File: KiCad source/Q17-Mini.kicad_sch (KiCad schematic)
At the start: 80 parts, among them J1 Input, J2-1 SPK+, J2-2 SPK-, J3-1 V+, J3-2 GND, J3-3 V-, Q1 IRF610, Q10 KSA992, Q11 ZVP2106A, Q12 BD139, Q13 IRF610, Q14 IRF9610, Q15 FQA46N15, Q16 FQA36P15, Q2 KSA992, Q3 KSC1845, Q4 IRF9610, Q5 FQP3P20, Q6 FQP3N30, Q7 KSC1845, Q8 ZVN4206AV, Q9 ZVP2106A, U1 OPA1641

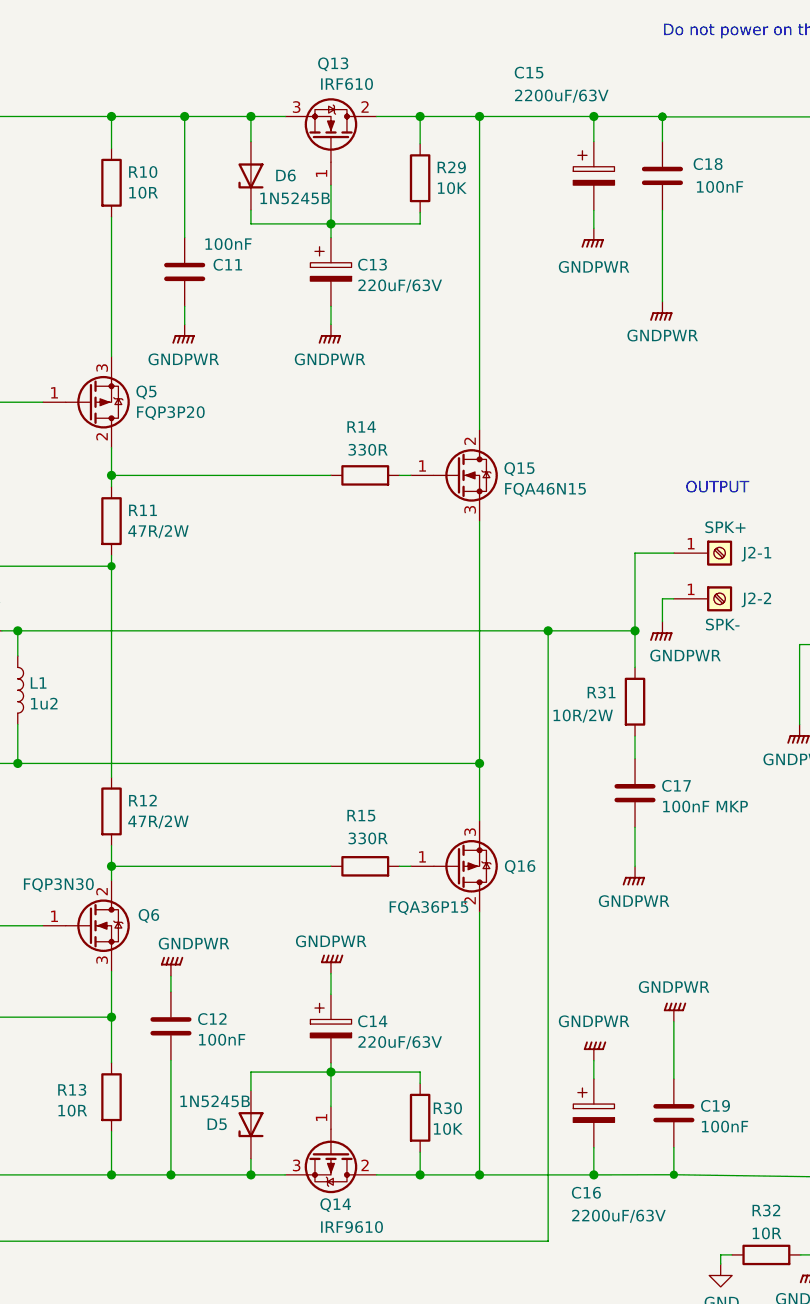
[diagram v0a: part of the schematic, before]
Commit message: Update Q17-Mini diagram
New 100R value for R29 and R30.
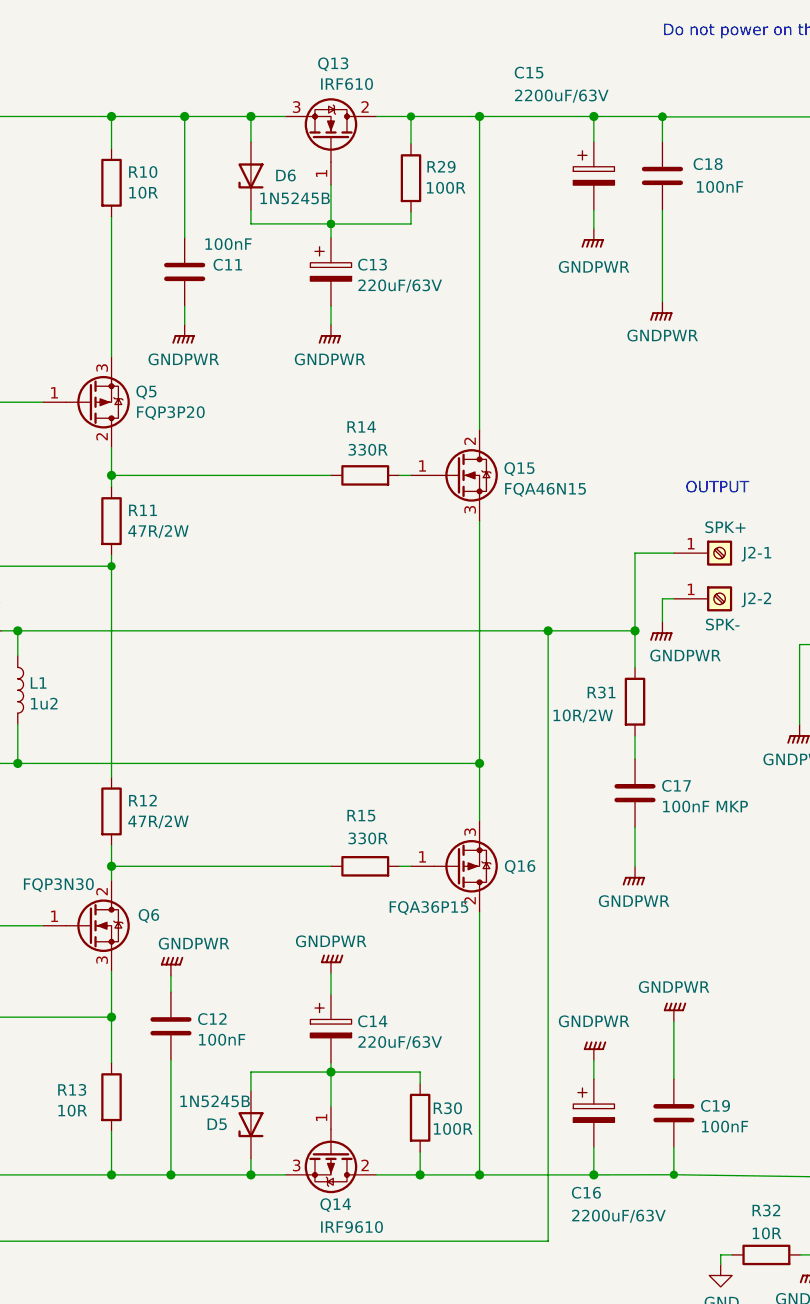
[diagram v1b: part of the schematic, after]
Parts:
- R29, R30: value 10K -> 100R
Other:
- moved on the sheet: R29
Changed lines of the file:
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@@
   (title_block
     (title "Q17-Mini Amplifier")
-    (date "2021-12-14")
-    (rev "1.1.4")
+    (date "2021-12-18")
+    (rev "1.1.5")
     (company "by eng. Tiberiu Vicol")
     (comment 1 "Modified by Stef for the Q17-Mini project")
@@
   (junction (at 49.53 103.124) (diameter 1.016) (color 0 0 0 0)
   )
+  (junction (at 203.2 35.8194) (diameter 0) (color 0 0 0 0)
+  )
   (junction (at 147.32 95.758) (diameter 1.016) (color 0 0 0 0)
   )
@@
   (junction (at 138.43 39.116) (diameter 1.016) (color 0 0 0 0)
   )
+  (junction (at 203.2 35.814) (diameter 0) (color 0 0 0 0)
+  )
   (junction (at 232.41 141.478) (diameter 1.016) (color 0 0 0 0)
   )
@@
   (junction (at 219.71 23.876) (diameter 1.016) (color 0 0 0 0)
   )
-  (junction (at 203.2 35.814) (diameter 1.016) (color 0 0 0 0)
-  )
   (junction (at 138.43 55.626) (diameter 1.016) (color 0 0 0 0)
   )
@@
   (junction (at 186.944 23.876) (diameter 1.016) (color 0 0 0 0)
   )
+  (junction (at 212.09 23.876) (diameter 0) (color 0 0 0 0)
+  )
   (junction (at 92.71 141.478) (diameter 1.016) (color 0 0 0 0)
   )
@@
   )
   (junction (at 42.672 73.914) (diameter 1.016) (color 0 0 0 0)
-  )
-  (junction (at 213.106 23.876) (diameter 1.016) (color 0 0 0 0)
   )
   (junction (at 241.3 141.4597) (diameter 0) (color 0 0 0 0)
@@
     (stroke (width 0) (type solid) (color 0 0 0 0))
   )
-  (wire (pts (xy 213.106 23.876) (xy 213.106 26.924))
-    (stroke (width 0) (type solid) (color 0 0 0 0))
-  )
   (wire (pts (xy 49.53 96.774) (xy 49.53 103.124))
     (stroke (width 0) (type solid) (color 0 0 0 0))
@@
   )
   (wire (pts (xy 203.2 44.958) (xy 203.2 46.99))
-    (stroke (width 0) (type solid) (color 0 0 0 0))
-  )
-  (wire (pts (xy 203.2 31.496) (xy 203.2 35.814))
-    (stroke (width 0) (type solid) (color 0 0 0 0))
-  )
-  (wire (pts (xy 203.2 35.814) (xy 203.2 37.338))
-    (stroke (width 0) (type solid) (color 0 0 0 0))
-  )
-  (wire (pts (xy 203.2 35.814) (xy 213.106 35.814))
-    (stroke (width 0) (type solid) (color 0 0 0 0))
-  )
-  (wire (pts (xy 213.106 35.814) (xy 213.106 34.544))
     (stroke (width 0) (type solid) (color 0 0 0 0))
   )
@@
     (stroke (width 0) (type solid) (color 0 0 0 0))
   )
-  (wire (pts (xy 219.71 23.876) (xy 213.106 23.876))
-    (stroke (width 0) (type solid) (color 0 0 0 0))
-  )
   (wire (pts (xy 219.71 58.674) (xy 219.71 23.876))
     (stroke (width 0) (type solid) (color 0 0 0 0))
   )
-  (wire (pts (xy 213.106 23.876) (xy 208.28 23.876))
+  (wire (pts (xy 208.28 23.876) (xy 212.09 23.876))
     (stroke (width 0) (type solid) (color 0 0 0 0))
   )
@@
     (stroke (width 0) (type solid) (color 0 0 0 0))
   )
+  (wire (pts (xy 203.2 31.496) (xy 203.2 35.814))
+    (stroke (width 0) (type default) (color 0 0 0 0))
+  )
   (wire (pts (xy 260.35 88.9) (xy 260.35 141.732))
     (stroke (width 0) (type solid) (color 0 0 0 0))
@@
     (stroke (width 0) (type solid) (color 0 0 0 0))
   )
+  (wire (pts (xy 212.09 35.8194) (xy 212.0909 34.5405))
+    (stroke (width 0) (type default) (color 0 0 0 0))
+  )
   (wire (pts (xy 116.332 80.01) (xy 116.332 83.312))
     (stroke (width 0) (type solid) (color 0 0 0 0))
@@
   )
   (wire (pts (xy 67.818 23.876) (xy 78.994 23.876))
+    (stroke (width 0) (type solid) (color 0 0 0 0))
+  )
+  (wire (pts (xy 212.09 23.876) (xy 219.71 23.876))
     (stroke (width 0) (type solid) (color 0 0 0 0))
   )
@@
     (stroke (width 0) (type solid) (color 0 0 0 0))
   )
+  (wire (pts (xy 203.2 35.8194) (xy 212.09 35.8194))
+    (stroke (width 0) (type default) (color 0 0 0 0))
+  )
   (wire (pts (xy 67.818 141.478) (xy 78.994 141.478))
     (stroke (width 0) (type solid) (color 0 0 0 0))
@@
   (wire (pts (xy 78.994 117.856) (xy 78.994 116.586))
     (stroke (width 0) (type solid) (color 0 0 0 0))
+  )
+  (wire (pts (xy 203.2 35.8194) (xy 203.2 37.338))
+    (stroke (width 0) (type default) (color 0 0 0 0))
   )
   (wire (pts (xy 150.368 55.626) (xy 150.368 58.166))
@@
     (stroke (width 0) (type solid) (color 0 0 0 0))
   )
+  (wire (pts (xy 203.2 35.814) (xy 203.2 35.8194))
+    (stroke (width 0) (type default) (color 0 0 0 0))
+  )
   (wire (pts (xy 178.816 73.8461) (xy 178.816 97.282))
     (stroke (width 0) (type solid) (color 0 0 0 0))
@@
   (wire (pts (xy 116.332 93.472) (xy 116.332 95.758))
     (stroke (width 0) (type solid) (color 0 0 0 0))
+  )
+  (wire (pts (xy 212.0909 26.9205) (xy 212.09 23.876))
+    (stroke (width 0) (type default) (color 0 0 0 0))
   )
   (wire (pts (xy 186.944 44.958) (xy 186.944 46.99))
@@
     (pin "1")
   )
-  (symbol (lib_id "Device:R") (at 213.106 30.734 0) (unit 1)
-    (in_bom yes) (on_board yes)
-    (property "Reference" "R29" (id 0) (at 214.8841 29.5846 0)
-      (effects (font (size 1.27 1.27)) (justify left))
-    )
-    (property "Value" "10K" (id 1) (at 214.884 31.883 0)
-      (effects (font (size 1.27 1.27)) (justify left))
-    )
-    (property "Footprint" "Resistor_THT:R_Axial_DIN0207_L6.3mm_D2.5mm_P10.16mm_Horizontal" (id 2) (at 211.328 30.734 90)
-      (effects (font (size 1.27 1.27)) hide)
-    )
-    (property "Datasheet" "~" (id 3) (at 213.106 30.734 0)
+  (symbol (lib_id "Device:R") (at 212.0909 30.7305 0) (unit 1)
+    (in_bom yes) (on_board yes)
+    (property "Reference" "R29" (id 0) (at 213.7392 29.5145 0)
+      (effects (font (size 1.27 1.27)) (justify left))
+    )
+    (property "Value" "100R" (id 1) (at 213.6614 31.8491 0)
+      (effects (font (size 1.27 1.27)) (justify left))
+    )
+    (property "Footprint" "Resistor_THT:R_Axial_DIN0207_L6.3mm_D2.5mm_P10.16mm_Horizontal" (id 2) (at 210.3129 30.7305 90)
+      (effects (font (size 1.27 1.27)) hide)
+    )
+    (property "Datasheet" "~" (id 3) (at 212.0909 30.7305 0)
       (effects (font (size 1.27 1.27)) hide)
     )
@@
       (effects (font (size 1.27 1.27)) (justify left))
     )
-    (property "Value" "10K" (id 1) (at 214.4419 136.4182 0)
+    (property "Value" "100R" (id 1) (at 214.4419 136.4182 0)
       (effects (font (size 1.27 1.27)) (justify left))
     )
@@
     )
     (path "/6a502bca-5c03-4909-9915-ce87906e504a"
-      (reference "R29") (unit 1) (value "10K") (footprint "Resistor_THT:R_Axial_DIN0207_L6.3mm_D2.5mm_P10.16mm_Horizontal")
+      (reference "R29") (unit 1) (value "100R") (footprint "Resistor_THT:R_Axial_DIN0207_L6.3mm_D2.5mm_P10.16mm_Horizontal")
     )
     (path "/860cc2f6-176f-4935-b38a-f52437fa5513"
-      (reference "R30") (unit 1) (value "10K") (footprint "Resistor_THT:R_Axial_DIN0207_L6.3mm_D2.5mm_P10.16mm_Horizontal")
+      (reference "R30") (unit 1) (value "100R") (footprint "Resistor_THT:R_Axial_DIN0207_L6.3mm_D2.5mm_P10.16mm_Horizontal")
     )
     (path "/0b38258b-fc2c-4616-935a-ea7f37c299ab"

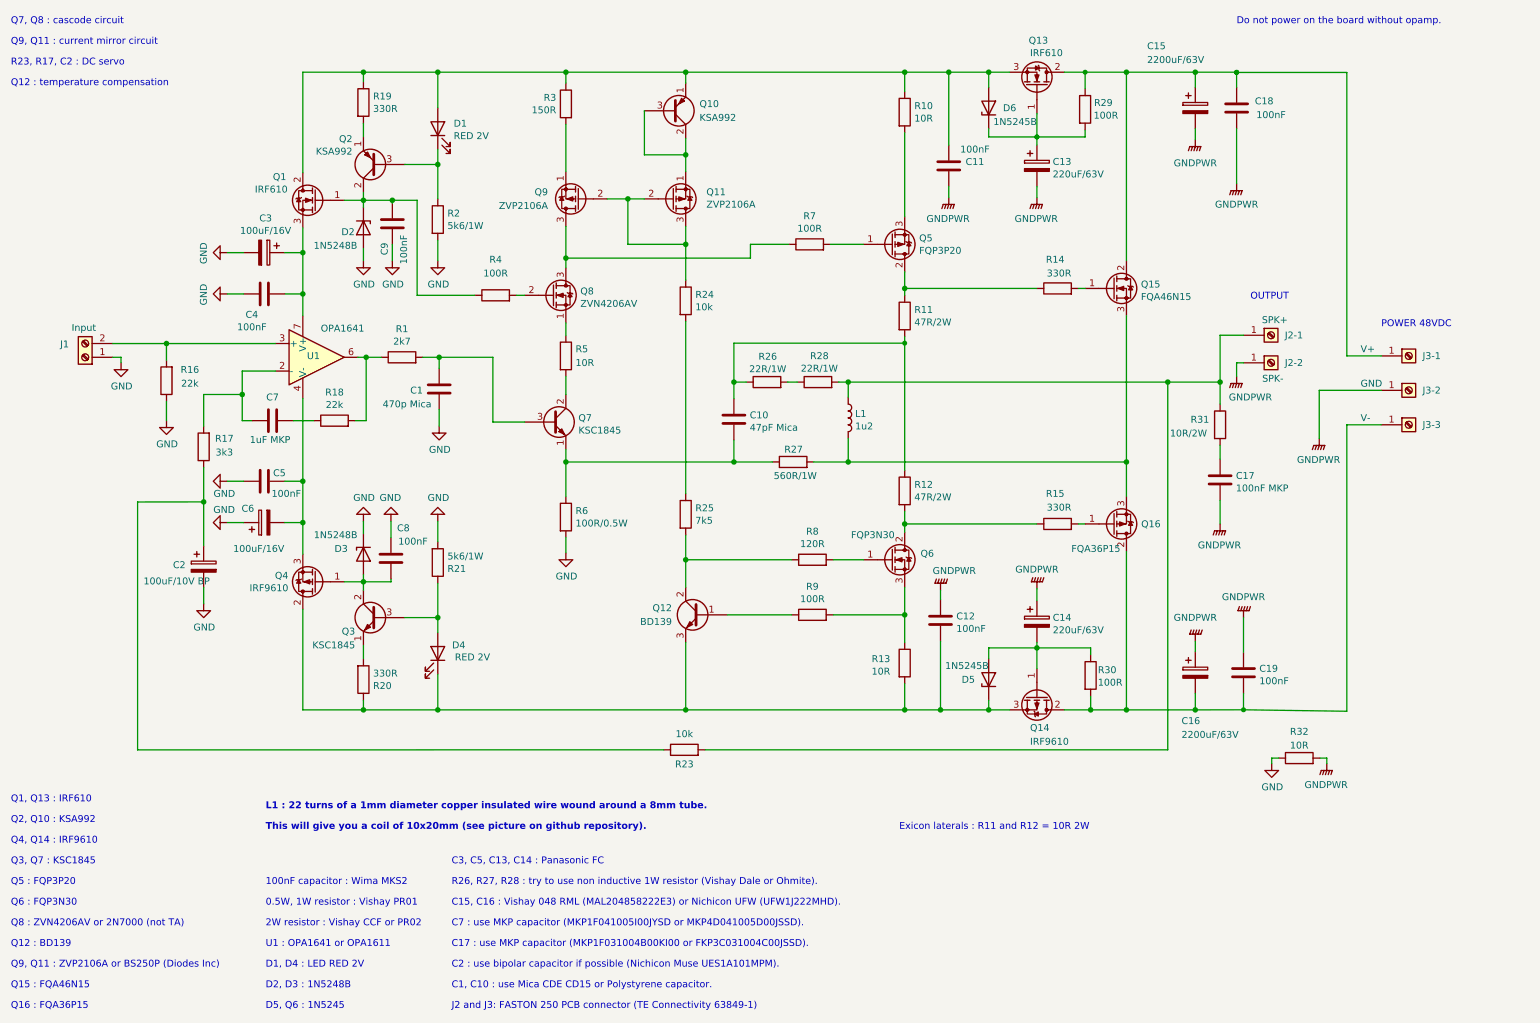
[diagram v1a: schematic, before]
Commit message: Update Q17-MIni diagram
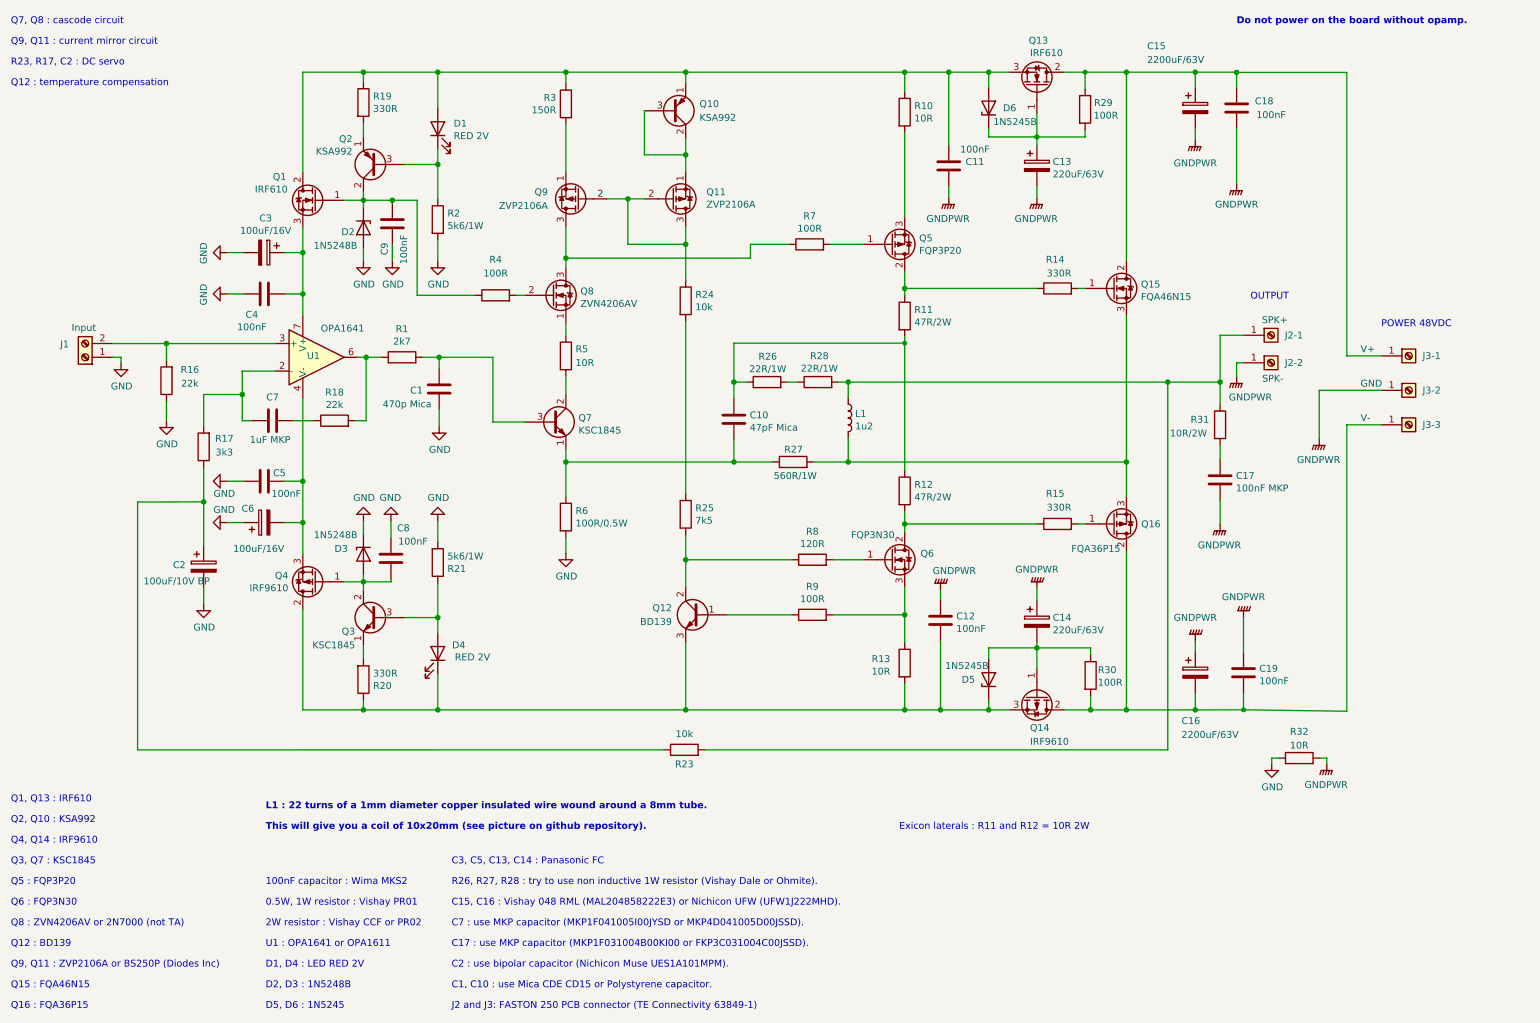
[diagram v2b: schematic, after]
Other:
- note added: "C2 : use bipolar capacitor (Nichicon Muse UES1A101MPM)."
- note added: "D5, D6 : 1N5245"
- note removed: "C2 : use bipolar capacitor if possible (Nichicon Muse UES1A101MPM)."
- note removed: "D5, Q6 : 1N5245"
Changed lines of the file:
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@@
   (title_block
     (title "Q17-Mini Amplifier")
-    (date "2021-12-18")
-    (rev "1.1.5")
+    (date "2021-12-21")
+    (rev "1.1.7")
     (company "by eng. Tiberiu Vicol")
     (comment 1 "Modified by Stef for the Q17-Mini project")
@@
     (effects (font (size 1.27 1.27)) (justify left bottom))
   )
-  (text "C2 : use bipolar capacitor if possible (Nichicon Muse UES1A101MPM)."
+  (text "C2 : use bipolar capacitor (Nichicon Muse UES1A101MPM)."
     (at 95.25 189.23 0)
     (effects (font (size 1.27 1.27)) (justify left bottom))
@@
     (effects (font (size 1.27 1.27)) (justify left bottom))
   )
-  (text "D5, Q6 : 1N5245" (at 60.96 196.85 0)
+  (text "D5, D6 : 1N5245" (at 60.96 196.85 0)
     (effects (font (size 1.27 1.27)) (justify left bottom))
   )
   (text "Do not power on the board without opamp." (at 240.03 15.24 0)
-    (effects (font (size 1.27 1.27)) (justify left bottom))
+    (effects (font (size 1.27 1.27) (thickness 0.254) bold) (justify left bottom))
   )
   (text "100nF capacitor : Wima MKS2" (at 60.96 173.99 0)

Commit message: Update diagrams with fuse values
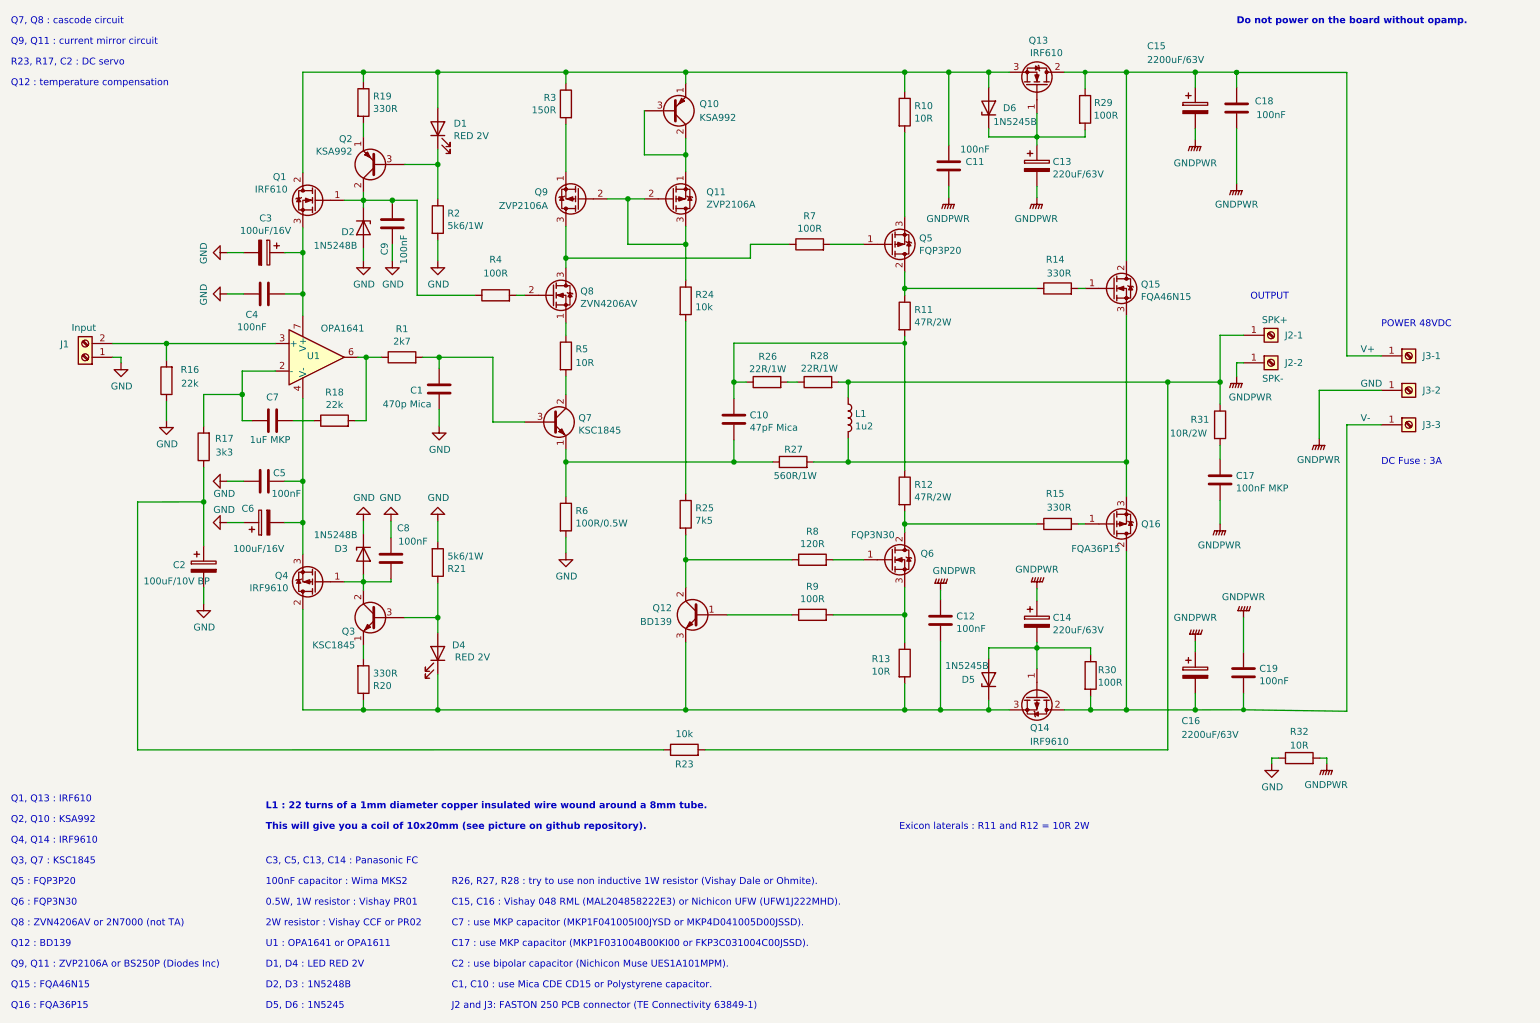
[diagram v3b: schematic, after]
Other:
- note added: "DC Fuse : 3A"
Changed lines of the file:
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@@
   (title_block
     (title "Q17-Mini Amplifier")
-    (date "2021-12-21")
+    (date "2021-12-22")
     (rev "1.1.7")
     (company "by eng. Tiberiu Vicol")
@@
     (stroke (width 0) (type solid) (color 0 0 0 0))
   )
-  (text "C3, C5, C13, C14 : Panasonic FC " (at 95.25 170.18 0)
+  (text "C3, C5, C13, C14 : Panasonic FC " (at 60.96 170.18 0)
     (effects (font (size 1.27 1.27)) (justify left bottom))
   )
@@
     (effects (font (size 1.27 1.27) (thickness 0.254) bold) (justify left bottom))
   )
+  (text "DC Fuse : 3A" (at 266.7 96.52 0)
+    (effects (font (size 1.27 1.27)) (justify left bottom))
+  )
   (text "Exicon laterals : R11 and R12 = 10R 2W" (at 177.8 163.83 0)
